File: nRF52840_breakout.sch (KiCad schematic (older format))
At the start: 35 parts, among them J1 MM8930_2620, J7 Conn_Coaxial, U1 nRF52840, Y1 32.768kHz-SIT1533AI-H4-DCC-32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, Y2 32MHz-XRCGB32M000F1H00R0

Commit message: changes
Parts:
- removed J1: MM8930_2620, custom_footprints:MM8930_2620, symbol Connector:Conn_Coaxial
- removed Y1: 32.768kHz-SIT1533AI-H4-DCC-32.768E, Crystal:Crystal_SMD_2012-2Pin_2.0x1.2mm, symbol Device:Crystal
- added D?: LTST-C19HE1WT, custom_footprints:LTST-C19HE1WT, symbol LTST-C19HE1WT:LTST-C19HE1WT
- added R? (x3): 1.5k, symbol Device:R_Small
- added U5: MM8130-2600RA2, custom_footprints:MM8930_2620, symbol CONN_SWF:MM8130-2600RA2
- added Y1: SiT1533, custom_footprints:Crystal_SMD_2012-4Pin_2.2mmx1.4mm, symbol Device:Crystal_GND24_Small
- J7: footprint custom_footprints:MM8930_2620 -> custom_footprints:CON_AMP_A-1JB
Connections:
- net GND: now also U5.3 (GND), Y1.2
- net P1.08: now also R?.2
- net P1.09: now also R?.2
- net P1.10: now also R?.2
- net VDD_nRF: now also D?.4, Y1.4
- net at C17.2, L4.2: now also U5.2 (Out)
- net at U1.D2 (XL1/P0.00): now also Y1.3
- net at U1.F2 (XL2/P0.01): now also Y1.1
- net at U1.H23 (ANT): now also U5.1 (In)
- new net: D?.1, R?.1
- new net: D?.2, R?.1
- new net: D?.3, R?.1
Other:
- moved on the sheet: C17, C20, C21, C22, J7, L4, R11, R12

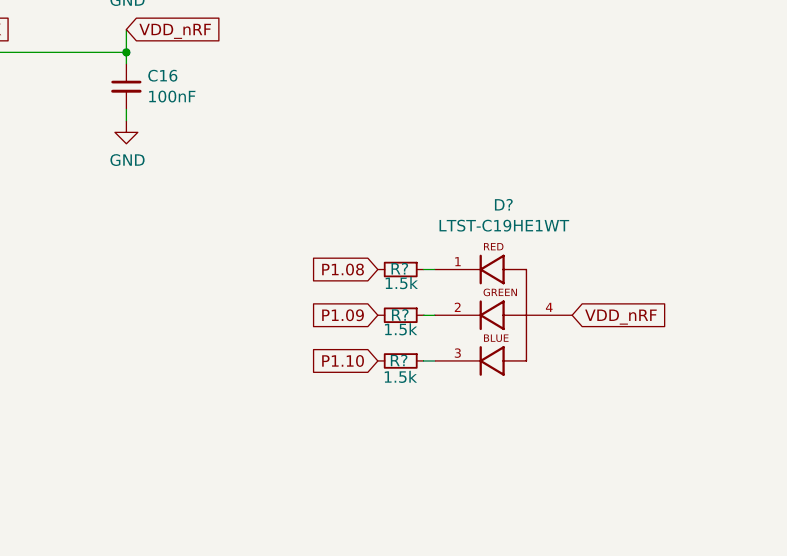
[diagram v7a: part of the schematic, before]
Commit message: minor changes / switched from tag - 10pol debug connector
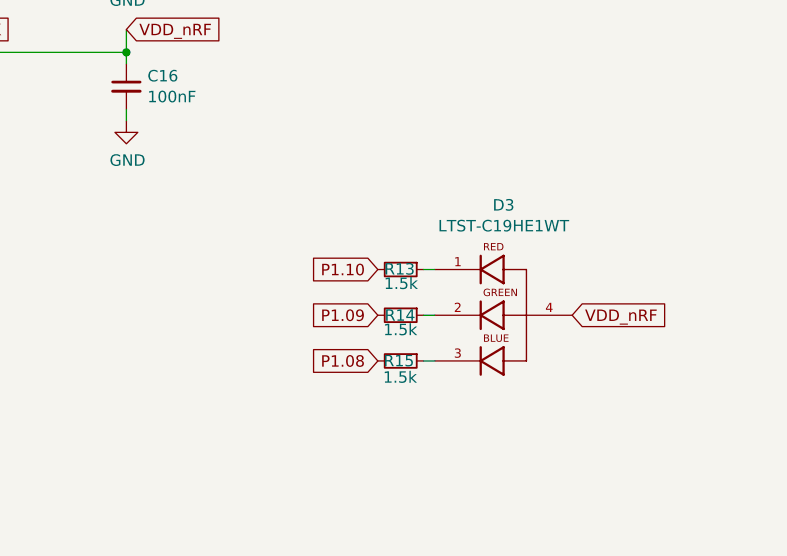
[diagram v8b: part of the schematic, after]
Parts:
- R13, R14, R15: renamed from R?; footprint (none) -> Resistor_SMD:R_0402_1005Metric
- gave numbers to parts that had none: 1
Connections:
- net P1.08: now also R15.2; no longer R13.2
- net P1.10: now also R13.2; no longer R15.2
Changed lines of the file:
@@
 Wire Wire Line
 	9550 5900 9500 5900
-Text GLabel 9300 5500 0    50   Input ~ 0
+Text GLabel 9300 5900 0    50   Input ~ 0
 P1.08
 Text GLabel 9300 5700 0    50   Input ~ 0
 P1.09
-Text GLabel 9300 5900 0    50   Input ~ 0
+Text GLabel 9300 5500 0    50   Input ~ 0
 P1.10
 $Comp
-L Device:R_Small R?
+L Device:R_Small R13
 U 1 1 5CDA0CC5
 P 9400 5500
-F 0 "R?" V 9399 5495 50  0000 C CNN
+F 0 "R13" V 9399 5495 50  0000 C CNN
 F 1 "1.5k" V 9462 5501 50  0000 C CNN
-F 2 "" H 9400 5500 50  0001 C CNN
+F 2 "Resistor_SMD:R_0402_1005Metric" H 9400 5500 50  0001 C CNN
 F 3 "~" H 9400 5500 50  0001 C CNN
 	1    9400 5500
@@
 $EndComp
 $Comp
-L Device:R_Small R?
+L Device:R_Small R14
 U 1 1 5CDA0D5D
 P 9400 5700
-F 0 "R?" V 9401 5697 50  0000 C CNN
+F 0 "R14" V 9401 5697 50  0000 C CNN
 F 1 "1.5k" V 9464 5698 50  0000 C CNN
-F 2 "" H 9400 5700 50  0001 C CNN
+F 2 "Resistor_SMD:R_0402_1005Metric" H 9400 5700 50  0001 C CNN
 F 3 "~" H 9400 5700 50  0001 C CNN
 	1    9400 5700
@@
 $EndComp
 $Comp
-L Device:R_Small R?
+L Device:R_Small R15
 U 1 1 5CDA0DBD
 P 9400 5900
-F 0 "R?" V 9400 5892 50  0000 C CNN
+F 0 "R15" V 9400 5892 50  0000 C CNN
 F 1 "1.5k" V 9472 5897 50  0000 C CNN
-F 2 "" H 9400 5900 50  0001 C CNN
+F 2 "Resistor_SMD:R_0402_1005Metric" H 9400 5900 50  0001 C CNN
 F 3 "~" H 9400 5900 50  0001 C CNN
 	1    9400 5900
@@
 $EndComp
 $Comp
-L LTST-C19HE1WT:LTST-C19HE1WT D?
+L LTST-C19HE1WT:LTST-C19HE1WT D3
 U 1 1 5CDACEAD
 P 9750 5700
-F 0 "D?" H 9850 6181 50  0000 C CNN
+F 0 "D3" H 9850 6181 50  0000 C CNN
 F 1 "LTST-C19HE1WT" H 9850 6090 50  0000 C CNN
 F 2 "custom_footprints:LTST-C19HE1WT" H 9750 5700 50  0001 L BNN
